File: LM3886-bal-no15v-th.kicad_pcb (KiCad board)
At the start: 2 copper layers, 69.1 x 40.6 mm, 29 parts, among them J1 IN, J2 OUT, J3 POWER, U1 LM3886

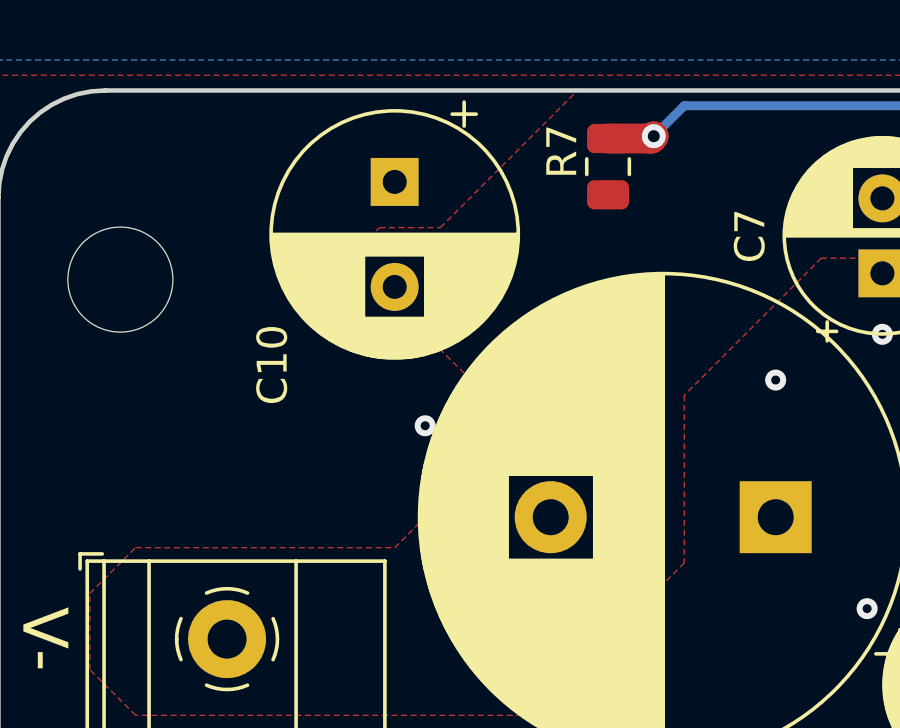
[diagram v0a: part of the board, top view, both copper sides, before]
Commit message: added imgs, fixed mute
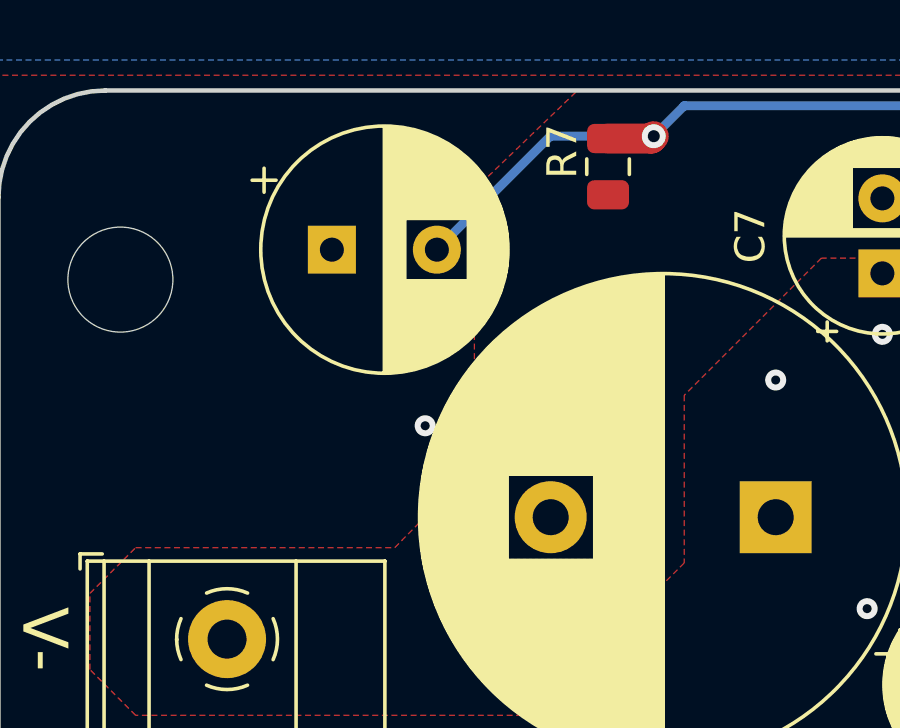
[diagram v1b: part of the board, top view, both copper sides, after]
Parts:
- C1: value 180p -> 220p
- R8: value 5.6R -> 6R8
- moved C10 3.08 mm to (83.2, 65.2), turned to 0 degrees
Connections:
- C10 pad 2: VEE -> /MUTE
- U1 pad 11: Net-(U1-Pad11) -> (no net)
- U1 pad 2: Net-(U1-Pad2) -> (no net)
- U1 pad 6: Net-(U1-Pad6) -> (no net)
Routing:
- net /MUTE: track 32.1 -> 40.9 mm

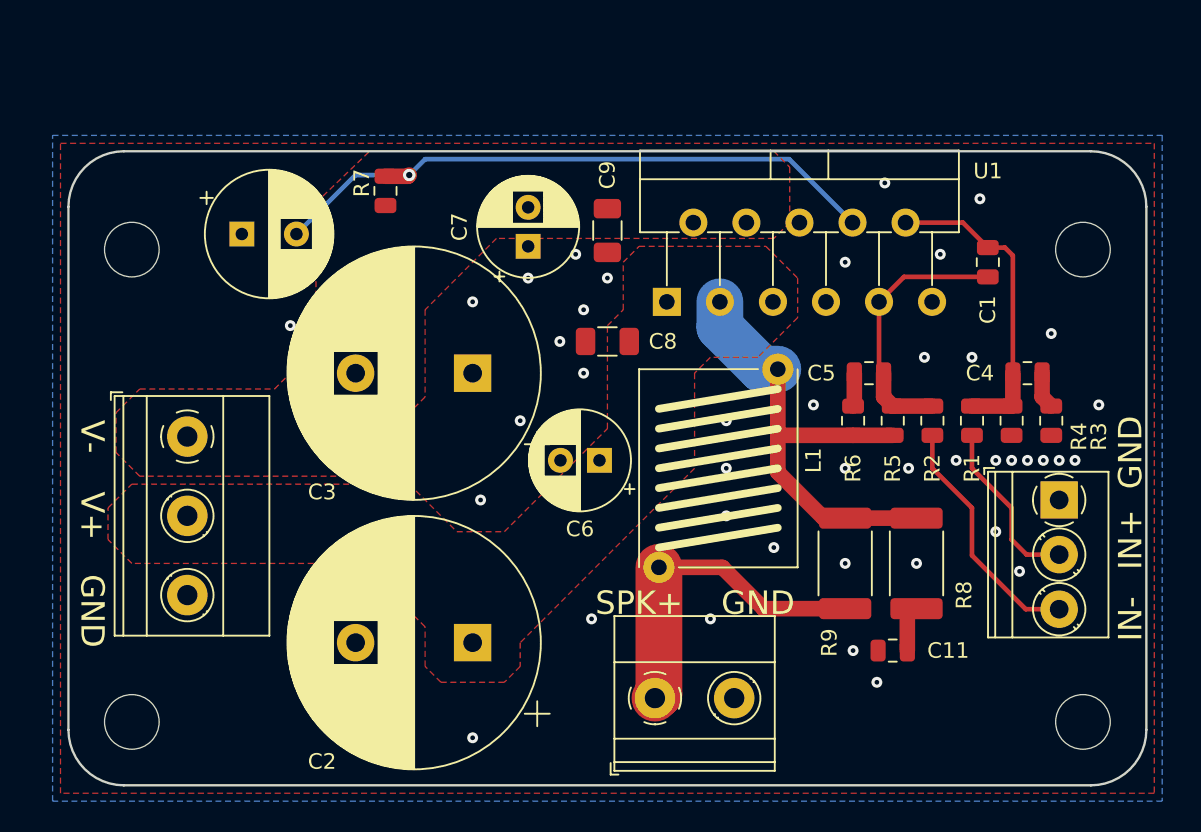
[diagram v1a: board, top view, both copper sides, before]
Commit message: fully new PCB layout
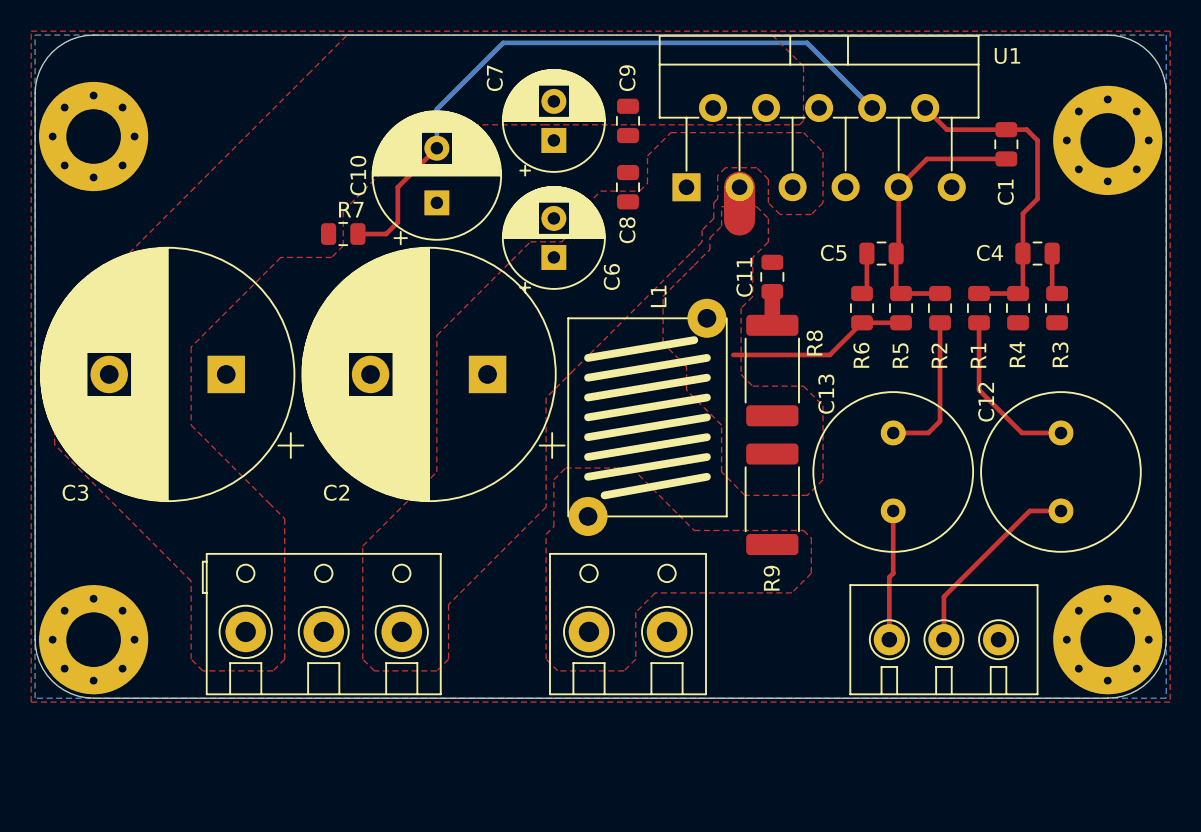
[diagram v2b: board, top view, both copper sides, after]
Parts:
- added C12: 100u NP, Capacitor_THT:C_Radial_D10.0mm_H12.5mm_P5.00mm, F.Cu at (135.8, 83.0)
- added C13: 100u NP, Capacitor_THT:C_Radial_D10.0mm_H12.5mm_P5.00mm, F.Cu at (125.0, 83.0)
- C8, C9: footprint Capacitor_SMD:C_1206_3216Metric -> Capacitor_SMD:C_0805_2012Metric
- H1, H2, H3, H4: footprint MountingHole:MountingHole_3.5mm -> MountingHole:MountingHole_3.5mm_Pad_Via
- J1: value IN -> INPUT; footprint TerminalBlock_Phoenix:TerminalBlock_Phoenix_PT-1,5-3-3.5-H_1x03_P3.50mm_Horizontal -> footprints:TerminalBlock_ Amphenol_01_03_P3.50mm
- J2: value OUT -> SPEAKER; footprint TerminalBlock_Phoenix:TerminalBlock_Phoenix_MKDS-1,5-2-5.08_1x02_P5.08mm_Horizontal-no1st -> footprints:TerminalBlock_CUI_01x02_P5.00mm
- J3: footprint TerminalBlock_Phoenix:TerminalBlock_Phoenix_MKDS-1,5-3-5.08_1x03_P5.08mm_Horizontal-no1st -> footprints:TerminalBlock_CUI_01x03_P5.00mm
- L1: footprint Inductor_THT:Inductor_DIY_flipped -> footprints:Inductor_DIY_flipped
- R8: value 6R8 -> 2R7 2W
- R9: value 10R -> 10R 2W
- moved C11 25.2 mm to (117.2, 68.0), turned to 90 degrees
- moved C2 17.2 mm to (99.0, 74.2)
- moved C3 15.8 mm to (82.2, 74.2)
- moved R8 15.4 mm to (117.2, 74.0), turned to 90 degrees
- moved J3 15.3 mm to (88.5, 90.8), turned to 0 degrees
- moved C6 13.3 mm to (103.2, 66.8), turned to 90 degrees
- moved C10 12.7 mm to (95.8, 63.2), turned to 90 degrees
- moved J1 11.6 mm to (128.2, 91.2), turned to 0 degrees
- moved C8 9.97 mm to (108.0, 62.2), turned to 90 degrees
- moved C5 7.71 mm to (124.2, 66.5)
- moved C4 7.70 mm to (134.2, 66.5)
- moved H1 7.65 mm to (73.8, 59.0)
- moved C1 7.65 mm to (132.2, 59.5)
- moved U1 7.45 mm to (111.8, 62.2)
- moved R6 7.24 mm to (123.0, 70.0)
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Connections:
- net Net-(J2-Pad1) renamed /SPK+
- J1 pad 1: GND -> Net-(C13-Pad1)
- J1 pad 2: /IN+ -> Net-(C12-Pad1)
- J1 pad 3: /IN- -> GND
- J3 pad 2: VCC -> GND
- J3 pad 3: GND -> VCC
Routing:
- net /SPK+: track 21.0 -> 0.00 mm
- net /SIGOUT: track 30.6 -> 13.7 mm
- net Net-(C12-Pad1): track 0.00 -> 12.5 mm
- net Net-(C13-Pad1): track 0.00 -> 8.35 mm
- net /IN-: track 15.8 -> 9.62 mm
- net /MUTE: track 40.9 -> 42.5 mm, vias 1 -> 0
- net /ICIN+: track 20.0 -> 20.9 mm
- net Net-(C11-Pad1): track 2.72 -> 2.16 mm
- net Net-(C5-Pad1): track 2.14 -> 2.69 mm
- net GND: vias 42 -> 0
- added copper zone on F.Cu, net /SIGOUT
- added copper zone on F.Cu, net /SPK+
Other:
- board size 69.1 x 40.6 mm -> 72.5 x 42.5 mm
- net class Default: clearance 0.2 -> 0.3; trace_width 0.25 -> 0.3; via_dia 0.8 -> 0.7; via_drill 0.4 -> 0.3
- rule trace_clearance: 0.2 -> 0.3
- board text removed: "GND"
- board text removed: "IN+"
- board text removed: "IN-"
- board text removed: "SPK+"
- board text removed: "V+"
- board text removed: "V-"
